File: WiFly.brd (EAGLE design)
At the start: 44.1 x 32.4 mm, 33 parts

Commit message: I honestly forgot what I updated
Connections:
- removed net N$5: U$2.12
- net GND: now also U$2.12
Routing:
- net GND: track 0.00 -> 3.92 mm, vias 0 -> 16
- net GPIO2: track 57.2 -> 55.4 mm
- net TX: track 14.2 -> 15.3 mm, vias 1 -> 0
- net RX: track 17.8 -> 18.4 mm, vias 1 -> 0
- added copper zone on layer 1, net GND
- added copper zone on layer 16, net GND
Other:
- board size 44.1 x 32.4 mm -> 45.7 x 34.3 mm
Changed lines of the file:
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@@
 <board>
 <plain>
-<wire x1="0" y1="0" x2="44.12" y2="0" width="0" layer="20"/>
-<wire x1="44.12" y1="0" x2="44.12" y2="32.375" width="0" layer="20"/>
-<wire x1="44.12" y1="32.375" x2="0" y2="32.375" width="0" layer="20"/>
-<wire x1="0" y1="32.375" x2="0" y2="0" width="0" layer="20"/>
+<wire x1="-0.635" y1="-0.9525" x2="45.0725" y2="-0.9525" width="0" layer="20"/>
+<wire x1="45.0725" y1="-0.9525" x2="45.0725" y2="33.3275" width="0" layer="20"/>
+<wire x1="45.0725" y1="33.3275" x2="-0.635" y2="33.3275" width="0" layer="20"/>
+<wire x1="-0.635" y1="33.3275" x2="-0.635" y2="-0.9525" width="0" layer="20"/>
 </plain>
 <attributes>
@@
 </element>
 <element name="JP3" library="adafruit" library_urn="urn:adsk.eagle:library:420" package="1X03-CLEANBIG" package3d_urn="urn:adsk.eagle:package:6240706/1" value="" x="38.1" y="30.48" smashed="yes">
-<attribute name="NAME" x="35.0012" y="26.5938" size="1.27" layer="25" ratio="10" rot="R90"/>
+<attribute name="NAME" x="34.6837" y="26.5938" size="1.27" layer="25" ratio="10" rot="R90"/>
 <attribute name="VALUE" x="34.29" y="27.305" size="1.27" layer="27"/>
 </element>
@@
 <contactref element="U$3" pad="5"/>
 <contactref element="-" pad="1"/>
-<wire x1="41.49" y1="24.13" x2="41.59" y2="26.205" width="0" layer="19" extent="1-1"/>
-<wire x1="41.39" y1="21.59" x2="41.49" y2="24.13" width="0" layer="19" extent="1-1"/>
-<wire x1="37.465" y1="12.915" x2="41.39" y2="21.59" width="0" layer="19" extent="1-1"/>
-<wire x1="35.56" y1="11.545" x2="37.465" y2="12.915" width="0" layer="19" extent="1-1"/>
-<wire x1="40.175" y1="7.305" x2="37.465" y2="12.915" width="0" layer="19" extent="1-1"/>
-<wire x1="30.16" y1="2.075" x2="35.56" y2="11.545" width="0" layer="19" extent="1-1"/>
-<wire x1="25.185" y1="1.905" x2="30.16" y2="2.075" width="0" layer="19" extent="1-1"/>
-<wire x1="22.86" y1="5.08" x2="25.185" y2="1.905" width="0" layer="19" extent="1-1"/>
-<wire x1="30.795" y1="28.11" x2="41.59" y2="26.205" width="0" layer="19" extent="1-1"/>
-<wire x1="23.915" y1="30.48" x2="30.795" y2="28.11" width="0" layer="19" extent="1-1"/>
-<wire x1="7.62" y1="9.525" x2="22.86" y2="5.08" width="0" layer="19" extent="1-1"/>
-<wire x1="1.79" y1="6.35" x2="7.62" y2="9.525" width="0" layer="19" extent="1-1"/>
-<wire x1="1.905" y1="19.685" x2="7.62" y2="9.525" width="0" layer="19" extent="1-1"/>
-<wire x1="3.29" y1="26.035" x2="1.905" y2="19.685" width="0" layer="19" extent="1-1"/>
-<wire x1="7.62" y1="27.94" x2="3.29" y2="26.035" width="0" layer="19" extent="1-1"/>
-<wire x1="31.115" y1="17.145" x2="1.79" y2="6.35" width="0" layer="19" extent="1-1"/>
+<polygon width="0.4064" layer="16" isolate="0.254">
+<vertex x="-0.635" y="-0.9525"/>
+<vertex x="-0.635" y="33.3375"/>
+<vertex x="45.085" y="33.3375"/>
+<vertex x="45.085" y="-0.9525"/>
+</polygon>
+<polygon width="0.4064" layer="1" isolate="0.254">
+<vertex x="-0.635" y="-0.9525"/>
+<vertex x="-0.635" y="33.3375"/>
+<vertex x="45.085" y="33.3375"/>
+<vertex x="45.085" y="-0.9525"/>
+</polygon>
+<via x="3.175" y="7.62" extent="1-16" drill="0.35"/>
+<wire x1="3.175" y1="7.62" x2="3.175" y2="8.5725" width="0.4064" layer="16"/>
+<wire x1="3.175" y1="8.5725" x2="3.4925" y2="8.89" width="0.4064" layer="16"/>
+<wire x1="3.4925" y1="8.89" x2="3.4925" y2="11.34475" width="0.4064" layer="16"/>
+<wire x1="3.4925" y1="11.34475" x2="3.449875" y2="11.387375" width="0.4064" layer="16"/>
+<via x="16.51" y="3.175" extent="1-16" drill="0.35"/>
+<via x="40.64" y="15.24" extent="1-16" drill="0.35"/>
+<via x="40.9575" y="17.78" extent="1-16" drill="0.35"/>
+<via x="24.765" y="13.0175" extent="1-16" drill="0.35"/>
+<via x="25.4" y="20.32" extent="1-16" drill="0.35"/>
+<via x="16.8275" y="20.0025" extent="1-16" drill="0.35"/>
+<via x="16.1925" y="13.0175" extent="1-16" drill="0.35"/>
+<via x="12.3825" y="20.32" extent="1-16" drill="0.35"/>
+<via x="8.5725" y="13.0175" extent="1-16" drill="0.35"/>
+<via x="2.54" y="24.13" extent="1-16" drill="0.35"/>
+<via x="7.9375" y="24.765" extent="1-16" drill="0.35"/>
+<via x="7.3025" y="22.86" extent="1-16" drill="0.35"/>
+<via x="35.8775" y="5.08" extent="1-16" drill="0.35"/>
+<via x="39.37" y="3.4925" extent="1-16" drill="0.35"/>
+<via x="42.2275" y="15.5575" extent="1-16" drill="0.35"/>
+<contactref element="U$2" pad="12"/>
 </signal>
 <signal name="N$2">
@@
 <wire x1="32.385" y1="30.1625" x2="32.385" y2="30.21" width="0.762" layer="1"/>
 <wire x1="29.845" y1="30.1625" x2="29.845" y2="30.31" width="0.762" layer="1"/>
-<wire x1="26.9875" y1="30.00375" x2="29.5275" y2="30.00375" width="0.762" layer="1"/>
-<wire x1="26.3525" y1="30.63875" x2="9.04875" y2="30.63875" width="0.762" layer="16"/>
-<wire x1="26.3525" y1="30.63875" x2="26.9875" y2="30.00375" width="0.762" layer="16"/>
+<wire x1="29.845" y1="30.31" x2="29.51625" y2="30.63875" width="0.762" layer="1"/>
+<wire x1="29.51625" y1="30.63875" x2="27.6225" y2="30.63875" width="0.762" layer="1"/>
+<wire x1="27.6225" y1="30.63875" x2="9.04875" y2="30.63875" width="0.762" layer="16"/>
 <wire x1="8.89" y1="30.48" x2="9.04875" y2="30.63875" width="0.762" layer="16"/>
-<wire x1="29.5275" y1="30.00375" x2="29.845" y2="30.31" width="0.762" layer="1"/>
-<via x="26.9875" y="30.00375" extent="1-16" drill="0.35"/>
+<via x="27.6225" y="30.63875" extent="1-16" drill="0.35"/>
 </signal>
 <signal name="VCC" class="1">
@@
 <contactref element="U$3" pad="1"/>
 <wire x1="33.81375" y1="2.2225" x2="31.75" y2="2.2225" width="0.762" layer="1"/>
-<wire x1="36.67125" y1="5.08" x2="33.81375" y2="2.2225" width="0.762" layer="1"/>
-<wire x1="38.37" y1="5.08" x2="36.67125" y2="5.08" width="0.762" layer="1"/>
+<wire x1="35.08375" y1="3.4925" x2="33.81375" y2="2.2225" width="0.762" layer="1"/>
+<wire x1="38.37" y1="5.08" x2="36.7825" y2="3.4925" width="0.762" layer="1"/>
+<wire x1="36.7825" y1="3.4925" x2="35.08375" y2="3.4925" width="0.762" layer="1"/>
 <wire x1="31.75" y1="2.2225" x2="31.75" y2="2.175" width="0.762" layer="1"/>
 <wire x1="38.1" y1="4.7625" x2="38.1" y2="1.905" width="0.762" layer="1"/>
@@
 <wire x1="15.24" y1="5.08" x2="10.795" y2="9.525" width="0.4064" layer="16"/>
 </signal>
-<signal name="N$5">
-<contactref element="U$2" pad="12"/>
-</signal>
 <signal name="N$6">
 <contactref element="R4" pad="2"/>
@@
 <contactref element="U$2" pad="14"/>
 <contactref element="U$3" pad="3"/>
-<wire x1="4.60375" y1="17.30375" x2="1.905" y2="14.605" width="0.4064" layer="1"/>
-<wire x1="4.60375" y1="19.84375" x2="4.60375" y2="17.30375" width="0.4064" layer="16"/>
-<wire x1="12.7" y1="27.94" x2="4.60375" y2="19.84375" width="0.4064" layer="16"/>
-<via x="4.60375" y="17.30375" extent="1-16" drill="0.35"/>
+<wire x1="1.905" y1="14.605" x2="3.4925" y2="16.1925" width="0.4064" layer="16"/>
+<wire x1="3.4925" y1="16.1925" x2="4.445" y2="16.1925" width="0.4064" layer="16"/>
+<wire x1="4.445" y1="16.1925" x2="12.7" y2="24.4475" width="0.4064" layer="16"/>
+<wire x1="12.7" y1="24.4475" x2="12.7" y2="27.94" width="0.4064" layer="16"/>
 </signal>
 <signal name="TX">
 <contactref element="U$2" pad="15"/>
 <contactref element="U$3" pad="4"/>
-<wire x1="3.81" y1="19.05" x2="1.905" y2="17.145" width="0.4064" layer="1"/>
-<wire x1="3.81" y1="21.59" x2="3.81" y2="19.05" width="0.4064" layer="16"/>
-<wire x1="10.16" y1="27.94" x2="3.81" y2="21.59" width="0.4064" layer="16"/>
-<via x="3.81" y="19.05" extent="1-16" drill="0.35"/>
+<wire x1="1.905" y1="17.145" x2="3.81" y2="17.145" width="0.4064" layer="16"/>
+<wire x1="3.81" y1="17.145" x2="10.16" y2="23.495" width="0.4064" layer="16"/>
+<wire x1="10.16" y1="23.495" x2="10.16" y2="27.94" width="0.4064" layer="16"/>
 </signal>
 <signal name="GPIO14">
@@
 <wire x1="3.81" y1="30.48" x2="3.4925" y2="30.1625" width="0.4064" layer="1"/>
 <wire x1="3.4925" y1="27.94" x2="3.39" y2="27.94" width="0.4064" layer="1"/>
-<wire x1="26.455" y1="24.765" x2="16.03375" y2="24.765" width="0.4064" layer="1"/>
+<wire x1="26.455" y1="24.765" x2="13.81125" y2="24.765" width="0.4064" layer="1"/>
 <wire x1="26.455" y1="24.765" x2="27.09" y2="25.4" width="0.4064" layer="1"/>
-<wire x1="13.97" y1="26.82875" x2="16.03375" y2="24.765" width="0.4064" layer="16"/>
-<wire x1="13.97" y1="28.41625" x2="13.97" y2="26.82875" width="0.4064" layer="16"/>
+<wire x1="13.97" y1="24.92375" x2="13.81125" y2="24.765" width="0.4064" layer="16"/>
+<wire x1="13.97" y1="28.41625" x2="13.97" y2="24.92375" width="0.4064" layer="16"/>
 <wire x1="13.17625" y1="29.21" x2="13.97" y2="28.41625" width="0.4064" layer="16"/>
 <wire x1="5.08" y1="29.21" x2="13.17625" y2="29.21" width="0.4064" layer="16"/>
 <wire x1="3.81" y1="30.48" x2="5.08" y2="29.21" width="0.4064" layer="16"/>
-<via x="16.03375" y="24.765" extent="1-16" drill="0.35"/>
+<via x="13.81125" y="24.765" extent="1-16" drill="0.35"/>
 <wire x1="10.16" y1="5.08" x2="6.35" y2="8.89" width="0.4064" layer="16"/>
-<wire x1="6.35" y1="19.05" x2="12.065" y2="24.765" width="0.4064" layer="16"/>
-<wire x1="12.065" y1="24.765" x2="16.03375" y2="24.765" width="0.4064" layer="16"/>
-<wire x1="6.35" y1="8.89" x2="6.35" y2="19.05" width="0.4064" layer="16"/>
+<wire x1="6.35" y1="17.145" x2="13.81125" y2="24.60625" width="0.4064" layer="16"/>
+<wire x1="13.81125" y1="24.60625" x2="13.81125" y2="24.765" width="0.4064" layer="16"/>
+<wire x1="6.35" y1="8.89" x2="6.35" y2="17.145" width="0.4064" layer="16"/>
 </signal>
 <signal name="GPIO12">

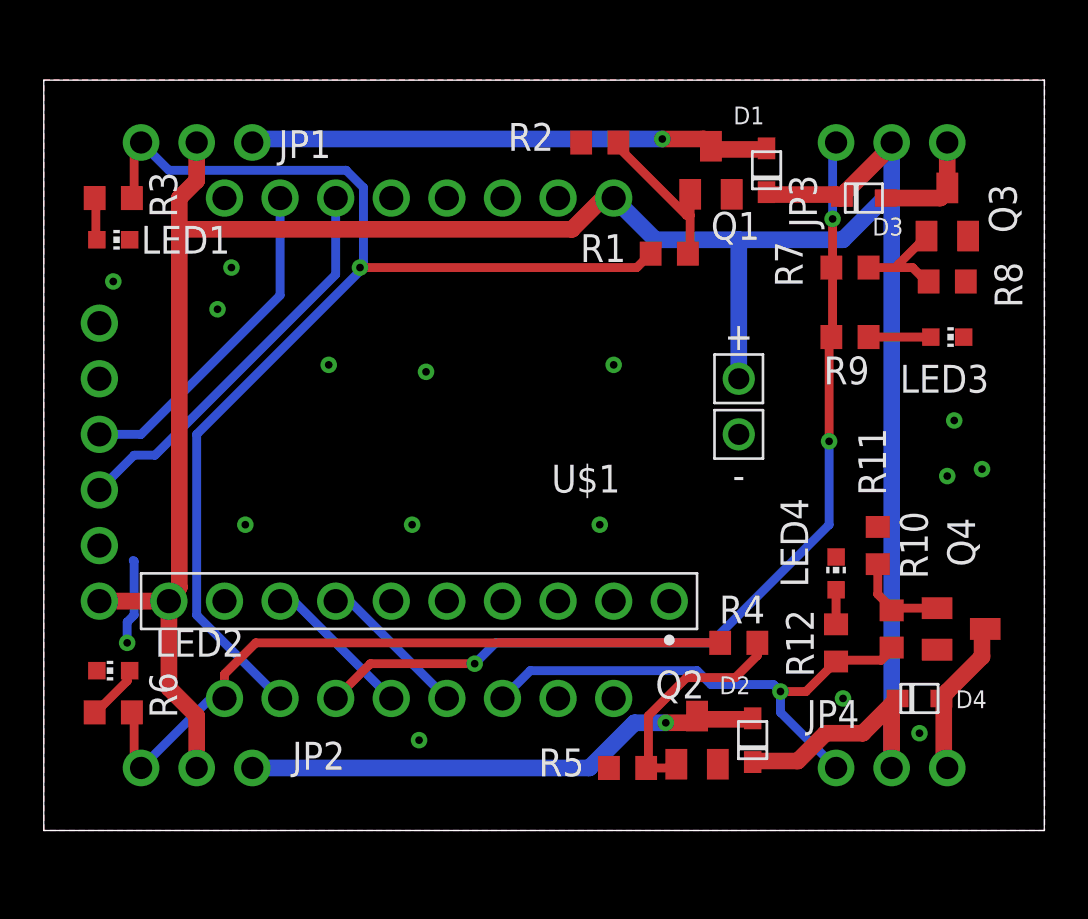
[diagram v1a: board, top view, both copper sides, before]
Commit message: Flipped ESP32CAM for physical layout, reworking other layouts
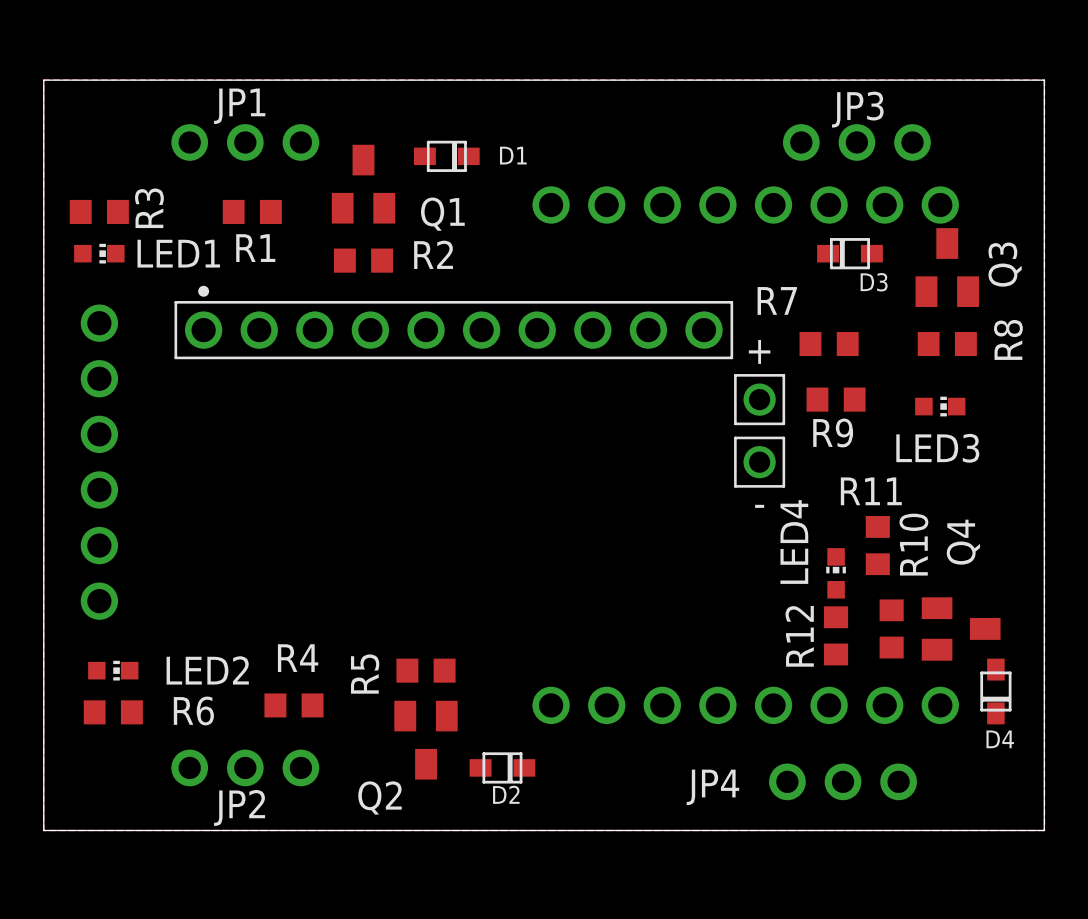
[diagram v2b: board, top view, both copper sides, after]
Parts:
- moved U$2 39.7 mm to (40.3, 27.6), turned to 0 degrees
- moved U$1 28.1 mm to (5.40, 23.2), turned to 0 degrees
- moved R4 20.5 mm to (10.8, 4.76)
- moved R1 19.1 mm to (8.89, 27.3)
- moved Q1 15.9 mm to (14.0, 28.6)
- moved D1 14.6 mm to (17.8, 29.8), turned to 0 degrees
- moved Q2 12.4 mm to (16.8, 3.17), turned to 180 degrees
- moved R2 12.1 mm to (14.0, 25.1), turned to 180 degrees
- moved D2 11.5 mm to (20.3, 1.91), turned to 0 degrees
- moved R5 10.2 mm to (16.8, 6.35)
- moved R7 3.62 mm to (35.2, 21.3)
- moved D4 3.51 mm to (42.9, 5.40), turned to 270 degrees
- moved LED3 3.19 mm to (40.3, 18.4)
- moved R9 2.93 mm to (35.6, 18.7)
- moved R8 2.86 mm to (40.6, 21.3)
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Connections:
- new net TODO1: JP4.1, R10.1, R12.2
- new net TODO2: JP3.1, R7.1, R9.2
- new net TODO3: JP2.1, R4.1, R6.2
- new net TODO4: JP1.1, R1.1, R3.2
- net GPIO12: no longer JP4.1, R10.1, R12.2
- net GPIO14: no longer JP3.1, R7.1, R9.2
- net GPIO2: no longer JP1.1, R1.1, R3.2
- net GPIO4: no longer JP2.1, R4.1, R6.2
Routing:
- net VCC: track 120.6 -> 0.00 mm
- net GPIO2: track 55.4 -> 0.00 mm, vias 1 -> 0
- net GPIO14: track 43.5 -> 0.00 mm, vias 3 -> 0
- net GPIO4: track 32.2 -> 0.00 mm
- net GPIO12: track 24.2 -> 0.00 mm, vias 1 -> 0
- net N$8: track 24.0 -> 0.00 mm, vias 1 -> 0
- net N$1: track 23.9 -> 0.00 mm, vias 1 -> 0
- net RX: track 18.4 -> 0.00 mm
- net TX: track 15.3 -> 0.00 mm
- net N$6: track 10.6 -> 0.00 mm
- net N$2: track 7.66 -> 0.00 mm
- net N$16: track 7.43 -> 0.00 mm
- net SDA: track 6.92 -> 0.00 mm
- net SCL: track 6.92 -> 0.00 mm
- net N$12: track 5.16 -> 0.00 mm
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
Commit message: Added mounting holes 9AWG 0.1144 in
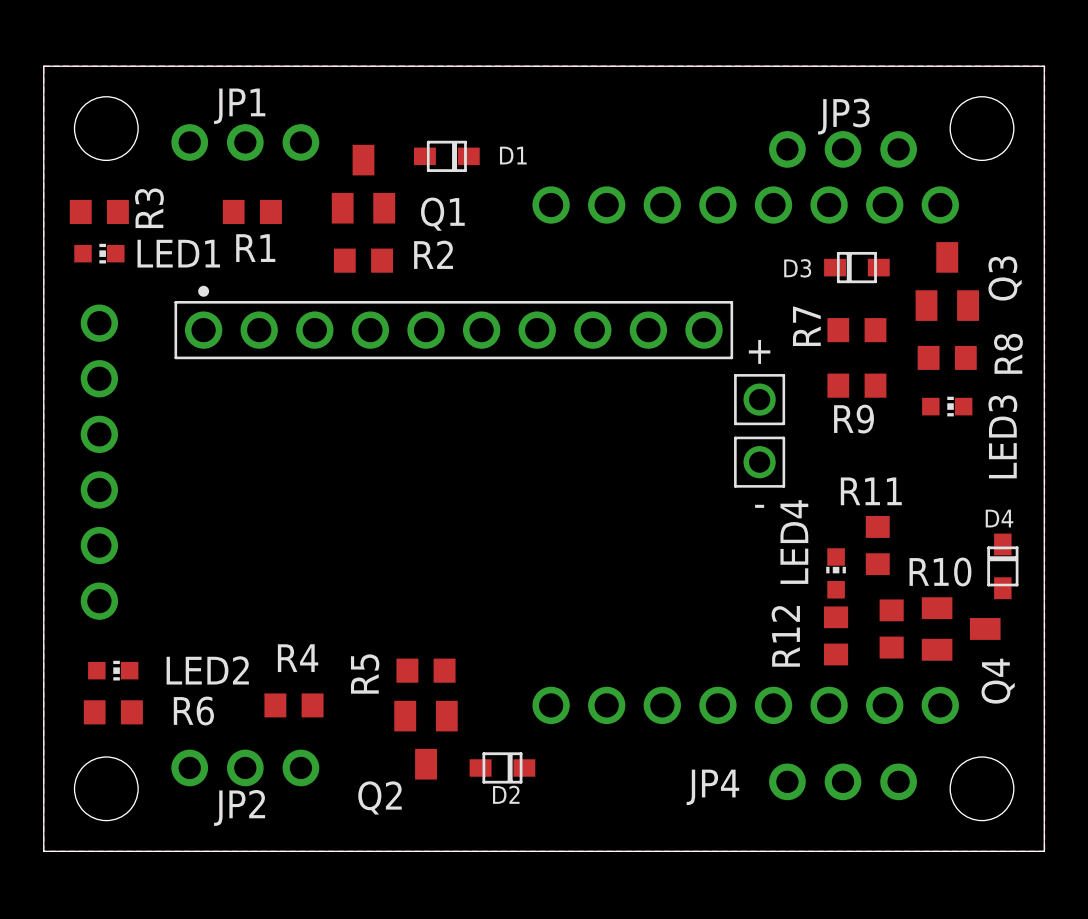
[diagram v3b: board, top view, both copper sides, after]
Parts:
- moved D4 5.72 mm to (43.2, 11.1), turned to 90 degrees
- moved R7 1.42 mm to (36.5, 21.9)
- moved R9 1.14 mm to (36.5, 19.4)
- moved JP3 0.71 mm to (35.9, 30.2)
- moved D3 0.71 mm to (36.5, 24.8)
- moved Q3 0.64 mm to (40.6, 24.1)
- moved R8 0.64 mm to (40.6, 20.6)
- moved LED3 0.32 mm to (40.6, 18.4)
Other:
- board size 45.7 x 34.3 mm -> 45.7 x 35.9 mm

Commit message: Initial routing, need to re-assign Motor Driver IO pins
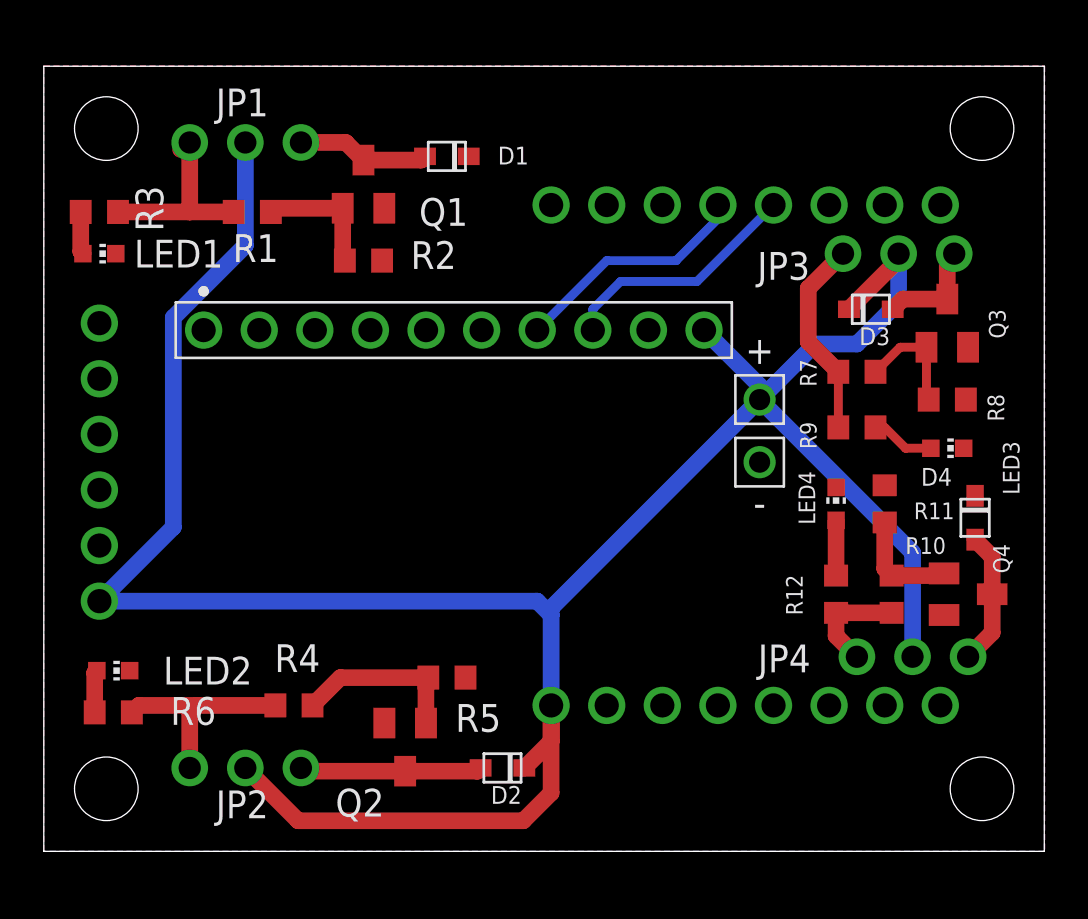
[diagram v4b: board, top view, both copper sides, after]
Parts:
- moved JP4 6.54 mm to (39.1, 6.99)
- moved JP3 5.40 mm to (38.4, 25.4)
- moved LED4 3.18 mm to (35.6, 14.0)
- moved D4 2.56 mm to (41.9, 13.3)
- moved D3 2.01 mm to (37.1, 22.9)
- moved R11 1.93 mm to (37.8, 14.0)
- moved R9 1.91 mm to (36.5, 17.5)
- moved R12 1.90 mm to (35.6, 9.84)
- moved LED3 1.90 mm to (40.6, 16.5)
- moved Q3 1.90 mm to (40.6, 22.2)
- moved R7 1.90 mm to (36.5, 20.0)
- moved R8 1.90 mm to (40.6, 18.7)
- moved Q4 1.62 mm to (41.6, 9.84)
- moved R10 1.59 mm to (38.1, 9.84)
- moved Q2 1.00 mm to (15.9, 2.86)
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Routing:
- net VCC: track 0.00 -> 118.2 mm
- net SCL: track 0.00 -> 11.2 mm
- net SDA: track 0.00 -> 11.0 mm
- net TODO3: track 0.00 -> 9.68 mm
- net TODO2: track 0.00 -> 9.16 mm
- net TODO4: track 0.00 -> 9.01 mm
- net N$8: track 0.00 -> 8.33 mm
- net N$6: track 0.00 -> 7.93 mm
- net N$16: track 0.00 -> 6.13 mm
- net N$1: track 0.00 -> 6.07 mm
- net N$2: track 0.00 -> 5.78 mm
- net N$10: track 0.00 -> 5.23 mm
- net N$14: track 0.00 -> 4.99 mm
- net TODO1: track 0.00 -> 4.94 mm
- net N$12: track 0.00 -> 4.89 mm
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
